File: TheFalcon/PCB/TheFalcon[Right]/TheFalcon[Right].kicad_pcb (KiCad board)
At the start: 4 copper layers, 173.3 x 142.5 mm, 36 parts

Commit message: Save
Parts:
- added C1: 10u, Capacitor_SMD:C_0805_2012Metric, B.Cu at (170.6, 34.7)
- added C10: 22u, Capacitor_SMD:C_1206_3216Metric, B.Cu at (95.3, 32.8)
- added C11: 22u, Capacitor_SMD:C_1206_3216Metric, B.Cu at (95.5, 43.2)
- added C12: 10p, Capacitor_SMD:C_0402_1005Metric, B.Cu at (186.9, 36.5)
- added C13: 100n, Capacitor_SMD:C_0402_1005Metric, B.Cu at (205.1, 39.2)
- added C14: 10p, Capacitor_SMD:C_0402_1005Metric, B.Cu at (186.9, 38.8)
- added C15: 100n, Capacitor_SMD:C_0402_1005Metric, B.Cu at (172.8, 134.6)
- added C16: 100n, Capacitor_SMD:C_0402_1005Metric, B.Cu at (143.5, 134.1)
- added C17: 1u, Capacitor_SMD:C_0603_1608Metric, B.Cu at (141.9, 133.8)
- added C2: 100n, Capacitor_SMD:C_0402_1005Metric, B.Cu at (180.8, 31.8)
- added C3: 100n, Capacitor_SMD:C_0402_1005Metric, B.Cu at (175.4, 43.6)
- added C4: 100n, Capacitor_SMD:C_0402_1005Metric, B.Cu at (184.0, 34.5)
- added C5: 100n, Capacitor_SMD:C_0402_1005Metric, B.Cu at (172.2, 35.2)
- added C6: 10n, Capacitor_SMD:C_0402_1005Metric, B.Cu at (177.4, 46.6)
- added C7: 1u, Capacitor_SMD:C_0603_1608Metric, B.Cu at (177.4, 48.0)
- added C8: 100n, Capacitor_SMD:C_0402_1005Metric, B.Cu at (178.0, 43.8)
- added C9: 1u, Capacitor_SMD:C_0603_1608Metric, B.Cu at (178.4, 45.2)
- added D1: Diode, Diode_SMD:Nexperia_CFP3_SOD-123W, B.Cu at (212.6, 47.0)
- added D10: Diode, Diode_SMD:D_SOD-123, B.Cu at (174.1, 61.2)
- added D11: Diode, Diode_SMD:D_SOD-123, B.Cu at (155.0, 56.3)
- added D12: Diode, Diode_SMD:D_SOD-123, B.Cu at (135.9, 62.3)
- added D13: Diode, Diode_SMD:D_SOD-123, B.Cu at (117.3, 65.4)
- added D14: Diode, Diode_SMD:D_SOD-123, B.Cu at (98.0, 65.3)
- added D15: Diode, Diode_SMD:D_SOD-123, B.Cu at (212.5, 84.9)
- added D16: Diode, Diode_SMD:D_SOD-123, B.Cu at (193.5, 84.9)
- added D17: Diode, Diode_SMD:D_SOD-123, B.Cu at (174.4, 80.2)
- added D18: Diode, Diode_SMD:D_SOD-123, B.Cu at (155.0, 75.3)
- added D19: Diode, Diode_SMD:D_SOD-123, B.Cu at (136.0, 81.3)
- added D2: Diode, Diode_SMD:D_SOD-123, B.Cu at (193.3, 46.9)
- added D20: Diode, Diode_SMD:D_SOD-123, B.Cu at (117.1, 84.3)
- added D21: Diode, Diode_SMD:D_SOD-123, B.Cu at (98.0, 84.2)
- added D22: Diode, Diode_SMD:D_SOD-123, B.Cu at (212.8, 103.8)
- added D23: Diode, Diode_SMD:D_SOD-123, B.Cu at (193.5, 104.0)
- added D24: Diode, Diode_SMD:D_SOD-123, B.Cu at (174.2, 99.0)
- added D25: Diode, Diode_SMD:D_SOD-123, B.Cu at (155.4, 94.4)
- added D26: Diode, Diode_SMD:D_SOD-123, B.Cu at (136.1, 100.4)
- added D27: Diode, Diode_SMD:D_SOD-123, B.Cu at (117.0, 103.5)
- added D28: Diode, Diode_SMD:D_SOD-123, B.Cu at (97.8, 103.6)
- added D29: Diode, Diode_SMD:D_SOD-123, B.Cu at (212.1, 123.0)
- added D3: Diode, Diode_SMD:D_SOD-123, B.Cu at (174.2, 48.8)
- added D30: Diode, Diode_SMD:D_SOD-123, B.Cu at (193.4, 123.1)
- added D31: Diode, Diode_SMD:D_SOD-123, B.Cu at (174.1, 118.2)
- added D32: Diode, Diode_SMD:D_SOD-123, B.Cu at (155.3, 113.6)
- added D33: Diode, Diode_SMD:D_SOD-123, B.Cu at (136.0, 119.4)
- added D34: Diode, Diode_SMD:D_SOD-123, B.Cu at (113.3, 124.4)
- added D35: Diode, Diode_SMD:D_SOD-123, B.Cu at (94.7, 140.6)
- added D36: Diode, Diode_SMD:D_SOD-123, B.Cu at (73.9, 148.9)
- added D39: LED, LED_SMD:LED_0805_2012Metric, B.Cu at (103.6, 42.6)
- added D4: Diode, Diode_SMD:D_SOD-123, B.Cu at (154.7, 40.6)
- added D5: Diode, Diode_SMD:D_SOD-123, B.Cu at (136.1, 43.2)
- added D6: Diode, Diode_SMD:D_SOD-123, B.Cu at (117.0, 49.5)
- added D7: Diode, Diode_SMD:D_SOD-123, B.Cu at (98.2, 49.6)
- added D8: Diode, Diode_SMD:D_SOD-123, B.Cu at (212.6, 65.8)
- added D9: Diode, Diode_SMD:D_SOD-123, B.Cu at (193.3, 65.8)
- added F1: 500mA, Fuse:Fuse_1206_3216Metric, B.Cu at (88.1, 35.0)
- added H1: MountingHole_Pad, MountingHole:MountingHole_2.2mm_M2_Pad, B.Cu at (214.8, 35.3)
- added H2: MountingHole_Pad, MountingHole:MountingHole_2.2mm_M2_Pad, B.Cu at (230.1, 31.2)
- added H3: MountingHole_Pad, MountingHole:MountingHole_2.2mm_M2_Pad, B.Cu at (230.6, 2.30)
- added H4: MountingHole_Pad, MountingHole:MountingHole_2.2mm_M2_Pad, B.Cu at (230.6, 8.25)
- added H5: MountingHole_Pad, MountingHole:MountingHole_2.2mm_M2_Pad, B.Cu at (230.6, 14.2)
- added H6: MountingHole_Pad, MountingHole:MountingHole_2.2mm_M2_Pad, B.Cu at (230.6, 20.1)
- added IC1: IS31FL3729-QFLS4-TR, SamacSys_Parts:QFN40P400X400X80-33N-D, B.Cu at (146.8, 135.7)
- added J1: Conn_01x01, Connector_Wire:SolderWire-0.1sqmm_1x01_D0.4mm_OD1mm, B.Cu at (172.8, 16.9)
- added J2: Conn_01x01, Connector_Wire:SolderWire-0.1sqmm_1x01_D0.4mm_OD1mm, B.Cu at (172.8, 20.5)
- added J3: Conn_01x01, Connector_Wire:SolderWire-0.1sqmm_1x01_D0.4mm_OD1mm, B.Cu at (169.2, 16.9)
- added J4: Conn_01x01, Connector_Wire:SolderWire-0.1sqmm_1x01_D0.4mm_OD1mm, B.Cu at (169.2, 20.5)
- added J5: Conn_01x04_Pin, Connector_Wire:SolderWire-1sqmm_1x04_P5.4mm_D1.4mm_OD2.7mm, B.Cu at (175.3, 6.10)
- added J6: Conn_01x01, Connector_Wire:SolderWire-0.1sqmm_1x01_D0.4mm_OD1mm, B.Cu at (105.6, 32.9)
- added J7: Conn_01x01, Connector_Wire:SolderWire-0.1sqmm_1x01_D0.4mm_OD1mm, B.Cu at (100.9, 32.8)
- added J8: Conn_01x01, Connector_Wire:SolderWirePad_1x01_SMD_1x2mm, B.Cu at (144.0, 128.0)
- added R1: 20, Resistor_SMD:R_0603_1608Metric, B.Cu at (213.1, 55.6)
- added R10: 51, Resistor_SMD:R_0603_1608Metric, B.Cu at (212.6, 59.6)
- added R11: 20, Resistor_SMD:R_0603_1608Metric, B.Cu at (196.4, 78.1)
- added R12: 20, Resistor_SMD:R_0603_1608Metric, B.Cu at (194.1, 78.3)
- added R13: 51, Resistor_SMD:R_0603_1608Metric, B.Cu at (186.7, 82.6)
- added R14: 20, Resistor_SMD:R_0603_1608Metric, B.Cu at (139.0, 93.9)
- added R15: 20, Resistor_SMD:R_0603_1608Metric, B.Cu at (136.8, 95.1)
- added R16: 51, Resistor_SMD:R_0603_1608Metric, B.Cu at (129.1, 98.1)
- added R17: 20, Resistor_SMD:R_0603_1608Metric, B.Cu at (86.8, 124.3)
- added R18: 20, Resistor_SMD:R_0603_1608Metric, B.Cu at (92.6, 124.4)
- added R19: 51, Resistor_SMD:R_0603_1608Metric, B.Cu at (89.9, 124.4)
- added R2: 10k, Resistor_SMD:R_0603_1608Metric, B.Cu at (143.8, 131.4)
- added R20: 20, Resistor_SMD:R_0603_1608Metric, B.Cu at (159.3, 130.6)
- added R21: 20, Resistor_SMD:R_0603_1608Metric, B.Cu at (160.1, 133.2)
- added R22: 51, Resistor_SMD:R_0603_1608Metric, B.Cu at (160.1, 134.8)
- added R23: 0, Resistor_SMD:R_0603_1608Metric_Pad0.98x0.95mm_HandSolder, B.Cu at (143.6, 129.6)
- added R3: 4k7, Resistor_SMD:R_0603_1608Metric, B.Cu at (160.8, 36.8)
- added R4: 4k7, Resistor_SMD:R_0603_1608Metric, B.Cu at (162.4, 38.5)
- added R5: 1k5, Resistor_SMD:R_0603_1608Metric, B.Cu at (108.4, 42.6)
- added R6: 5.1k, Resistor_SMD:R_0603_1608Metric, B.Cu at (210.6, 36.4)
- added R7: 5.1k, Resistor_SMD:R_0603_1608Metric, B.Cu at (211.3, 38.9)
- added R8: 100k, Resistor_SMD:R_0603_1608Metric, B.Cu at (171.3, 134.9)
- added R9: 20, Resistor_SMD:R_0603_1608Metric, B.Cu at (213.2, 57.4)
- added RGB1: T36K3BGR-05D000121U1930, SamacSys_Parts:T36K3BGR05D000121U1930_MODEL_INVERTED, F.Cu at (205.4, 58.3)
- added RGB10: T36K3BGR-05D000121U1930, SamacSys_Parts:T36K3BGR05D000121U1930_MODEL_INVERTED, F.Cu at (167.5, 72.7)
- added RGB11: T36K3BGR-05D000121U1930, SamacSys_Parts:T36K3BGR05D000121U1930_MODEL_INVERTED, F.Cu at (148.4, 67.7)
- added RGB12: T36K3BGR-05D000121U1930, SamacSys_Parts:T36K3BGR05D000121U1930_MODEL_INVERTED, F.Cu at (129.3, 73.7)
- added RGB13: T36K3BGR-05D000121U1930, SamacSys_Parts:T36K3BGR05D000121U1930_MODEL_INVERTED, F.Cu at (110.2, 76.7)
- added RGB14: T36K3BGR-05D000121U1930, SamacSys_Parts:T36K3BGR05D000121U1930_MODEL_INVERTED, F.Cu at (91.1, 76.7)
- added RGB15: T36K3BGR-05D000121U1930, SamacSys_Parts:T36K3BGR05D000121U1930_MODEL_INVERTED, F.Cu at (205.7, 96.4)
- added RGB16: T36K3BGR-05D000121U1930, SamacSys_Parts:T36K3BGR05D000121U1930_MODEL_INVERTED, F.Cu at (186.6, 96.4)
- added RGB17: T36K3BGR-05D000121U1930, SamacSys_Parts:T36K3BGR05D000121U1930_MODEL_INVERTED, F.Cu at (167.5, 91.7)
- added RGB18: T36K3BGR-05D000121U1930, SamacSys_Parts:T36K3BGR05D000121U1930_MODEL_INVERTED, F.Cu at (148.4, 86.9)
- added RGB19: T36K3BGR-05D000121U1930, SamacSys_Parts:T36K3BGR05D000121U1930_MODEL_INVERTED, F.Cu at (129.3, 92.9)
- added RGB2: T36K3BGR-05D000121U1930, SamacSys_Parts:T36K3BGR05D000121U1930_MODEL_INVERTED, F.Cu at (186.3, 58.2)
- added RGB20: T36K3BGR-05D000121U1930, SamacSys_Parts:T36K3BGR05D000121U1930_MODEL_INVERTED, F.Cu at (110.2, 95.9)
- added RGB21: T36K3BGR-05D000121U1930, SamacSys_Parts:T36K3BGR05D000121U1930_MODEL_INVERTED, F.Cu at (91.3, 95.9)
- added RGB22: T36K3BGR-05D000121U1930, SamacSys_Parts:T36K3BGR05D000121U1930_MODEL_INVERTED, F.Cu at (205.7, 115.2)
- added RGB23: T36K3BGR-05D000121U1930, SamacSys_Parts:T36K3BGR05D000121U1930_MODEL_INVERTED, F.Cu at (186.3, 115.4)
- added RGB24: T36K3BGR-05D000121U1930, SamacSys_Parts:T36K3BGR05D000121U1930_MODEL_INVERTED, F.Cu at (167.5, 110.7)
- added RGB25: T36K3BGR-05D000121U1930, SamacSys_Parts:T36K3BGR05D000121U1930_MODEL_INVERTED, F.Cu at (148.1, 105.9)
- added RGB26: T36K3BGR-05D000121U1930, SamacSys_Parts:T36K3BGR05D000121U1930_MODEL_INVERTED, F.Cu at (129.3, 111.9)
- added RGB27: T36K3BGR-05D000121U1930, SamacSys_Parts:T36K3BGR05D000121U1930_MODEL_INVERTED, F.Cu at (110.2, 114.9)
- added RGB28: T36K3BGR-05D000121U1930, SamacSys_Parts:T36K3BGR05D000121U1930_MODEL_INVERTED, F.Cu at (91.1, 114.9)
- added RGB29: T36K3BGR-05D000121U1930, SamacSys_Parts:T36K3BGR05D000121U1930_MODEL_INVERTED, F.Cu at (205.4, 134.4)
- added RGB3: T36K3BGR-05D000121U1930, SamacSys_Parts:T36K3BGR05D000121U1930_MODEL_INVERTED, F.Cu at (167.5, 53.7)
- added RGB30: T36K3BGR-05D000121U1930, SamacSys_Parts:T36K3BGR05D000121U1930_MODEL_INVERTED, F.Cu at (186.3, 134.4)
- added RGB31: T36K3BGR-05D000121U1930, SamacSys_Parts:T36K3BGR05D000121U1930_MODEL_INVERTED, F.Cu at (167.2, 129.7)
- added RGB32: T36K3BGR-05D000121U1930, SamacSys_Parts:T36K3BGR05D000121U1930_MODEL_INVERTED, F.Cu at (148.4, 124.9)
- added RGB33: T36K3BGR-05D000121U1930, SamacSys_Parts:T36K3BGR05D000121U1930_MODEL_INVERTED, F.Cu at (129.3, 130.9)
- added RGB34: T36K3BGR-05D000121U1930, SamacSys_Parts:T36K3BGR05D000121U1930_MODEL_INVERTED, F.Cu at (106.6, 136.9)
- added RGB35: T36K3BGR-05D000121U1930, SamacSys_Parts:T36K3BGR05D000121U1930_MODEL_INVERTED, F.Cu at (80.8, 142.7)
- added RGB36: T36K3BGR-05D000121U1930, SamacSys_Parts:T36K3BGR05D000121U1930_MODEL_INVERTED, F.Cu at (60.4, 154.2)
- added RGB4: T36K3BGR-05D000121U1930, SamacSys_Parts:T36K3BGR05D000121U1930_MODEL_INVERTED, F.Cu at (148.4, 48.7)
- added RGB5: T36K3BGR-05D000121U1930, SamacSys_Parts:T36K3BGR05D000121U1930_MODEL_INVERTED, F.Cu at (129.3, 54.7)
- added RGB6: T36K3BGR-05D000121U1930, SamacSys_Parts:T36K3BGR05D000121U1930_MODEL_INVERTED, F.Cu at (110.4, 57.7)
- added RGB7: T36K3BGR-05D000121U1930, SamacSys_Parts:T36K3BGR05D000121U1930_MODEL_INVERTED, F.Cu at (91.3, 57.9)
- added RGB8: T36K3BGR-05D000121U1930, SamacSys_Parts:T36K3BGR05D000121U1930_MODEL_INVERTED, F.Cu at (205.5, 77.4)
- added RGB9: T36K3BGR-05D000121U1930, SamacSys_Parts:T36K3BGR05D000121U1930_MODEL_INVERTED, F.Cu at (186.6, 77.4)
- added SW1: SW_Push, Button_Switch_SMD:SW_SPST_B3U-1000P, B.Cu at (207.8, 37.2)
- added SW2: SW_Push, Button_Switch_SMD:SW_SPST_B3U-1000P, B.Cu at (202.5, 37.0)
- added U1: STM32G431CBTx, Package_QFP:LQFP-48_7x7mm_P0.5mm, B.Cu at (178.2, 37.8)
- added U3: USBLC6-2P6, Package_TO_SOT_SMD:SOT-666, B.Cu at (88.9, 37.8)
- added U4: AMS1117-3.3, Package_TO_SOT_SMD:SOT-223-3_TabPin2, B.Cu at (97.0, 38.1)
- added USB2: USB_C_Receptacle_USB2.0_16P, Connector_USB:USB_C_Receptacle_G-Switch_GT-USB-7010ASV, B.Cu at (79.6, 37.7)
- added Y1: X322516MOB4SI, SamacSys_Parts:X322516MOB4SI, B.Cu at (190.4, 37.0)
- moved S9 211.5 mm to (185.7, 72.1)
- moved S1 211.5 mm to (204.7, 53.1)
- moved S10 211.5 mm to (166.6, 67.3)
- moved S11 211.5 mm to (147.6, 62.6)
- moved S12 211.5 mm to (128.5, 68.6)
- moved S13 211.5 mm to (109.5, 71.6)
- moved S14 211.5 mm to (90.4, 71.6)
- moved S15 211.5 mm to (204.7, 91.2)
- moved S17 211.5 mm to (166.6, 86.4)
- moved S22 211.5 mm to (204.7, 110.2)
- moved S25 211.5 mm to (147.6, 100.7)
- moved S26 211.5 mm to (128.5, 106.7)
- moved S27 211.5 mm to (109.5, 109.7)
- moved S28 211.5 mm to (90.4, 109.7)
- moved S3 211.5 mm to (166.6, 48.3)
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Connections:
- S1 pad 1: Col0 -> Col6
- S10 pad 1: Col2 -> Col4
- S12 pad 1: Col4 -> Col2
- S13 pad 1: Col5 -> Col1
- S14 pad 1: Col6 -> Col0
- S15 pad 1: Col0 -> Col6
- S16 pad 1: Col1 -> Col5
- S17 pad 1: Col2 -> Col4
- S19 pad 1: Col4 -> Col2
- S2 pad 1: Col1 -> Col5
- S20 pad 1: Col5 -> Col1
- S21 pad 1: Col6 -> Col0
- S22 pad 1: Col0 -> Col6
- S23 pad 1: Col1 -> Col5
- S24 pad 1: Col2 -> Col4
- S26 pad 1: Col4 -> Col2
- S27 pad 1: Col5 -> Col1
- S28 pad 1: Col6 -> Col0
- S29 pad 1: Col0 -> Col6
- S3 pad 1: Col2 -> Col4
- S30 pad 1: Col1 -> Col5
- S31 pad 1: Col2 -> Col4
- S33 pad 1: Col4 -> Col2
- S34 pad 1: Col4 -> Col2
- S35 pad 1: Col5 -> Col1
- S36 pad 1: Col6 -> Col0
- S5 pad 1: Col4 -> Col2
- S6 pad 1: Col5 -> Col1
- S7 pad 1: Col6 -> Col0
- S8 pad 1: Col0 -> Col6
- S9 pad 1: Col1 -> Col5
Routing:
- net Row3: track 0.00 -> 235.3 mm, vias 0 -> 8
- net ThumbRow: track 0.00 -> 224.0 mm, vias 0 -> 2
- net Row4: track 0.00 -> 217.0 mm, vias 0 -> 6
- net Row2: track 0.00 -> 209.6 mm, vias 0 -> 8
- net /RGB Array/G_RGB_ROW_4: track 0.00 -> 208.7 mm, vias 0 -> 8
- net /RGB Array/R_RGB_ROW_4: track 0.00 -> 206.3 mm, vias 0 -> 9
- net Col0: track 0.00 -> 205.7 mm, vias 0 -> 2
- net /RGB Array/B_RGB_ROW_4: track 0.00 -> 202.9 mm, vias 0 -> 9
- net +3.3V: track 0.00 -> 181.4 mm, vias 0 -> 4
- net Col1: track 0.00 -> 180.9 mm, vias 0 -> 2
- net Row0: track 0.00 -> 173.7 mm, vias 0 -> 7
- net Row1: track 0.00 -> 171.4 mm, vias 0 -> 7
- net /RGB Array/G_RGB_ROW_3: track 0.00 -> 167.2 mm, vias 0 -> 7
- net +5V: track 0.00 -> 166.6 mm, vias 0 -> 5
- net /RGB Array/G_RGB_ROW_1: track 0.00 -> 157.2 mm, vias 0 -> 7
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- added copper zone on B.Cu, net +3.3V
- added copper zone on B.Cu, net +5V
- added copper zone on F.Cu, net +5V
- added copper zone on B.Cu, net GND
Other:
- board text added: "PA15"
- board text added: "X"

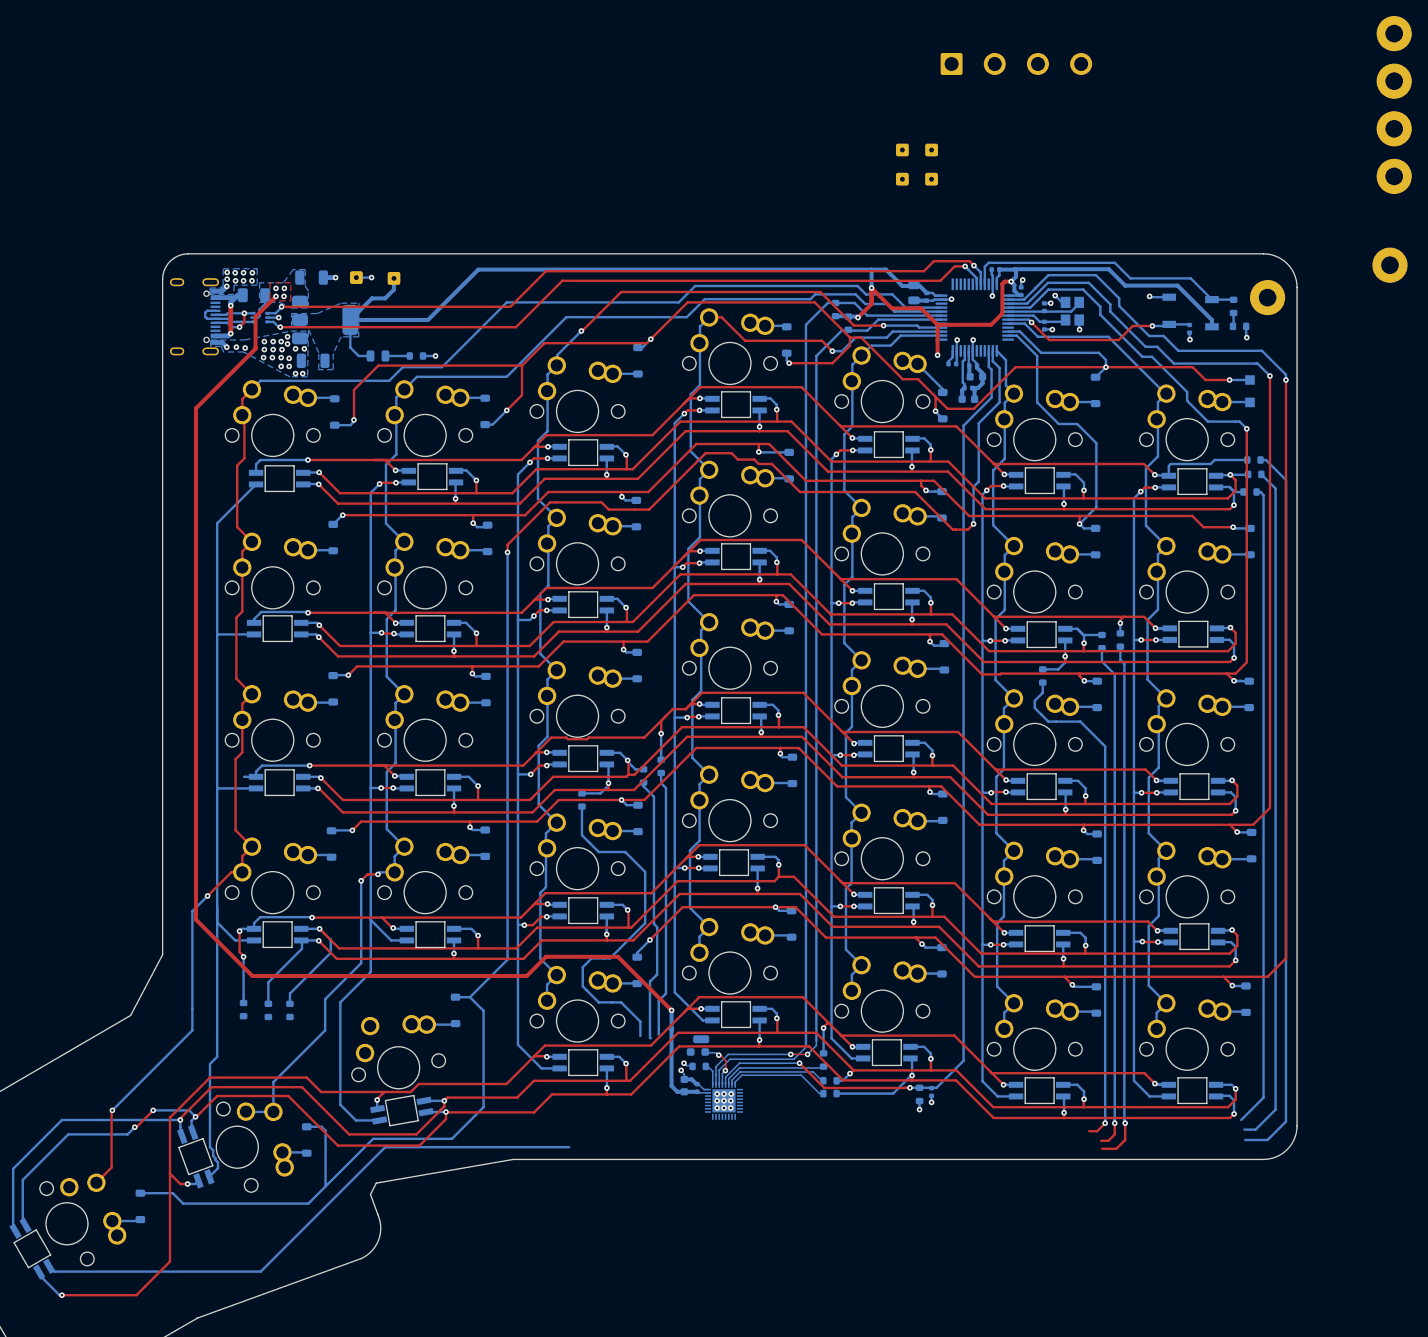
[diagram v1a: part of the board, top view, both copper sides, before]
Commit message: Right Side Done
Need to check but right side looks good
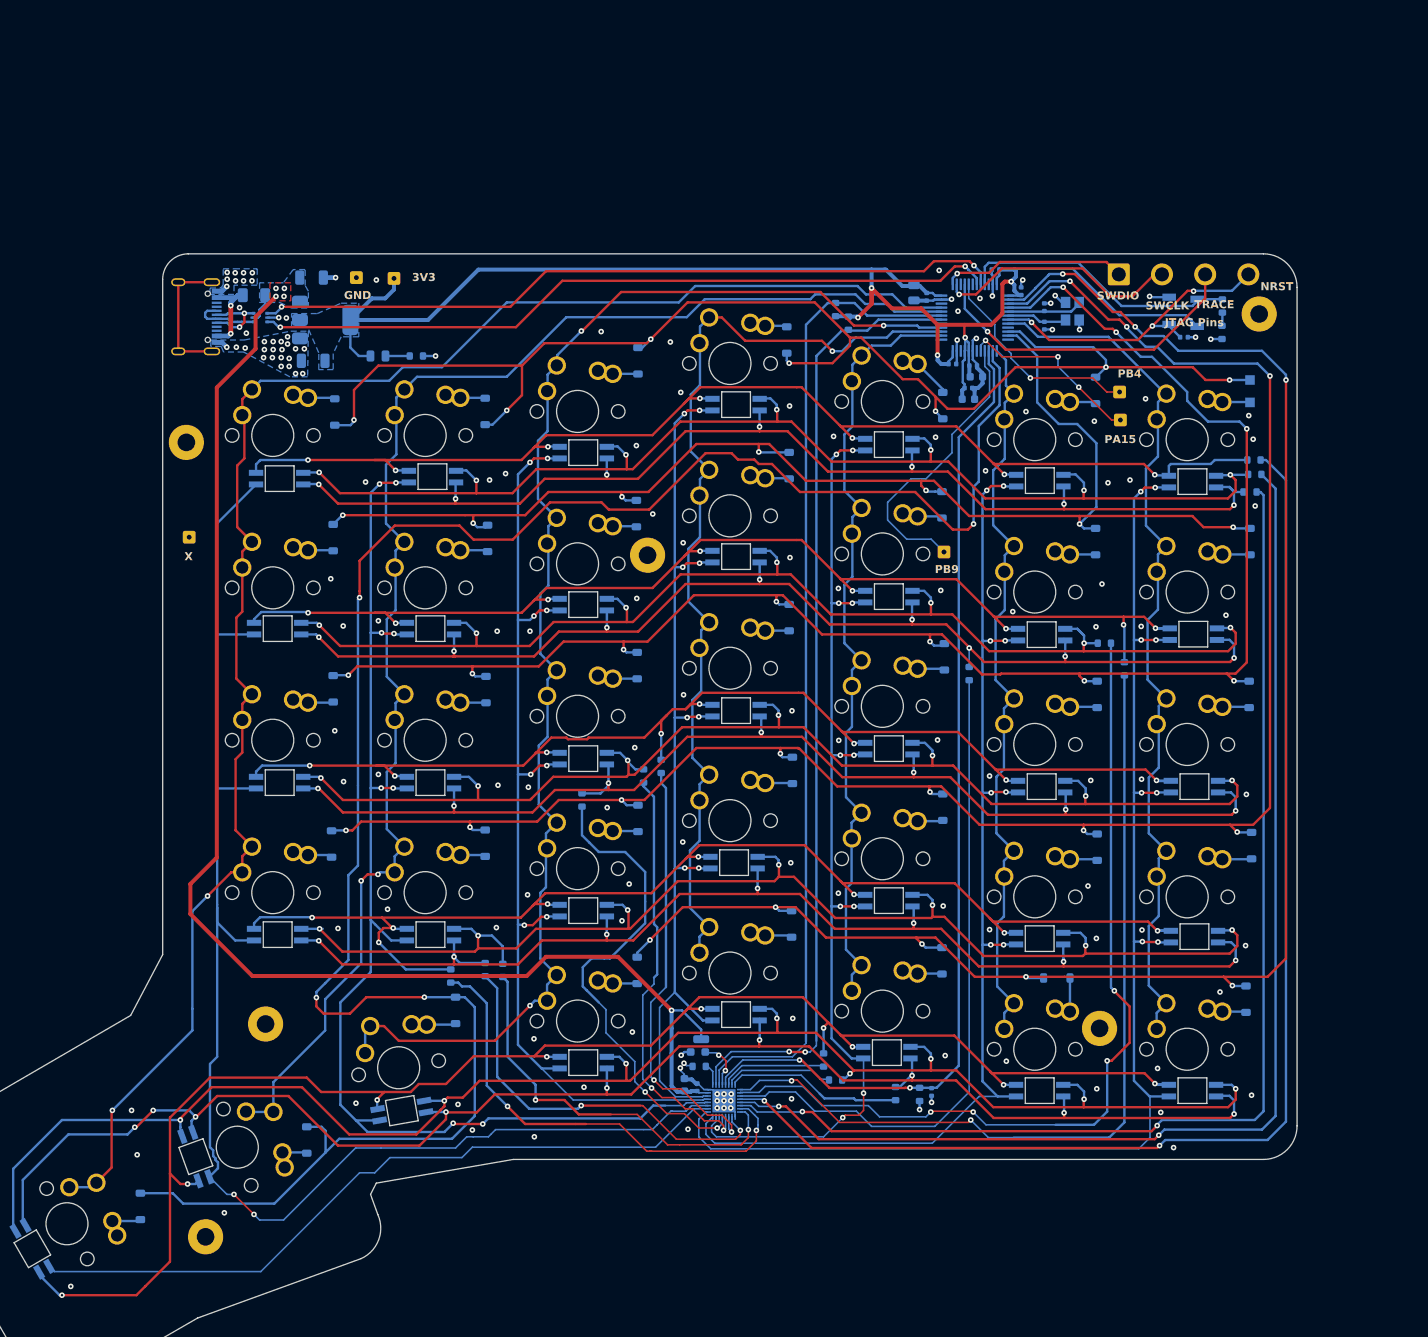
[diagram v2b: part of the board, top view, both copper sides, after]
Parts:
- moved H2 191.5 mm to (82.0, 152.7)
- moved H6 176.4 mm to (89.5, 126.1)
- moved H4 157.6 mm to (79.7, 53.4)
- moved H5 118.3 mm to (193.8, 126.7)
- moved H3 113.8 mm to (137.3, 67.5)
- moved J3 101.4 mm to (80.0, 65.2)
- moved J4 46.9 mm to (174.3, 67.1)
- moved J1 41.2 mm to (196.4, 50.6)
- moved J2 35.5 mm to (196.3, 47.1)
- moved J5 33.6 mm to (196.2, 32.4)
- moved R19 27.6 mm to (117.0, 119.3)
- moved R18 27.1 mm to (119.2, 119.4)
- moved R17 26.2 mm to (112.7, 120.1)
- moved R13 9.20 mm to (177.5, 82.3)
- moved R22 8.20 mm to (168.3, 134.8), turned to -90 degrees
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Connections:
- RGB1 pad 2: /RGB Array/SW8 -> /RGB Array/SW6
- RGB10 pad 2: /RGB Array/SW6 -> /RGB Array/SW8
- RGB11 pad 2: /RGB Array/SW5 -> /RGB Array/SW1
- RGB12 pad 2: /RGB Array/SW4 -> /RGB Array/SW2
- RGB14 pad 2: /RGB Array/SW2 -> /RGB Array/SW4
- RGB15 pad 2: /RGB Array/SW8 -> /RGB Array/SW6
- RGB17 pad 2: /RGB Array/SW6 -> /RGB Array/SW8
- RGB18 pad 2: /RGB Array/SW5 -> /RGB Array/SW1
- RGB19 pad 2: /RGB Array/SW4 -> /RGB Array/SW2
- RGB21 pad 2: /RGB Array/SW2 -> /RGB Array/SW4
- RGB22 pad 2: /RGB Array/SW8 -> /RGB Array/SW6
- RGB24 pad 2: /RGB Array/SW6 -> /RGB Array/SW8
- RGB25 pad 2: /RGB Array/SW5 -> /RGB Array/SW1
- RGB26 pad 2: /RGB Array/SW4 -> /RGB Array/SW2
- RGB28 pad 2: /RGB Array/SW2 -> /RGB Array/SW4
- RGB29 pad 2: /RGB Array/SW8 -> /RGB Array/SW6
- RGB3 pad 2: /RGB Array/SW6 -> /RGB Array/SW8
- RGB31 pad 2: /RGB Array/SW6 -> /RGB Array/SW8
- RGB32 pad 2: /RGB Array/SW5 -> /RGB Array/SW1
- RGB33 pad 2: /RGB Array/SW4 -> /RGB Array/SW2
- RGB35 pad 2: /RGB Array/SW2 -> /RGB Array/SW4
- RGB36 pad 2: /RGB Array/SW1 -> /RGB Array/SW5
- RGB4 pad 2: /RGB Array/SW5 -> /RGB Array/SW1
- RGB5 pad 2: /RGB Array/SW4 -> /RGB Array/SW2
- RGB7 pad 2: /RGB Array/SW2 -> /RGB Array/SW4
- RGB8 pad 2: /RGB Array/SW8 -> /RGB Array/SW6
- U1 pad 17: unconnected-(U1-PB1-Pad17) -> PA15
- U1 pad 39: PA15 -> unconnected-(U1-PA15-Pad39)
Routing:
- net /RGB Array/SW4: track 100.9 -> 177.2 mm, vias 8 -> 2
- net /RGB Array/SW6: track 94.8 -> 163.1 mm
- net /RGB Array/CS7: track 90.5 -> 156.6 mm, vias 0 -> 2
- net /RGB Array/CS8: track 85.1 -> 151.0 mm, vias 0 -> 2
- net /RGB Array/CS9: track 79.9 -> 145.6 mm, vias 0 -> 2
- net /RGB Array/CS10: track 0.00 -> 59.5 mm, vias 0 -> 2
- net /RGB Array/CS11: track 0.00 -> 50.4 mm, vias 0 -> 2
- net /RGB Array/CS12: track 0.00 -> 50.0 mm, vias 0 -> 2
- net /RGB Array/CS5: track 63.7 -> 110.5 mm, vias 1 -> 4
- net /RGB Array/SW3: track 103.8 -> 150.0 mm, vias 6 -> 8
- net /RGB Array/SW1: track 71.7 -> 115.7 mm, vias 0 -> 8
- net /RGB Array/CS4: track 65.6 -> 108.5 mm, vias 1 -> 2
- net /RGB Array/SW7: track 96.2 -> 138.1 mm
- net SYS_JTAG_TRACE: track 0.00 -> 40.9 mm, vias 0 -> 1
- net PB9: track 0.00 -> 36.5 mm
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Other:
- board text added: "3V3"
- board text added: "5V"
- board text added: "GND"
- board text added: "JTAG Pins"
- board text added: "NRST"
- board text added: "PB4"
- board text added: "PB9"
- board text added: "PWR"
- board text added: "SWCLK"
- board text added: "SWDIO"
- board text added: "TRACE"
- board text added: "USB Serial Connection"

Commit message: Save
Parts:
- removed H1, H2, H3, H4, H5, H6: MountingHole_Pad, MountingHole:MountingHole_2.2mm_M2_Pad
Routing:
- net unconnected-(USB2-SHIELD-PadS1): track 17.0 -> 0.00 mm
- net GND: track 55.7 -> 53.8 mm, vias 154 -> 153
- net /RGB Array/SW6: track 163.1 -> 164.4 mm
- net /RGB Array/SW2: track 123.4 -> 124.4 mm
- net /RGB Array/CS5: track 110.5 -> 111.3 mm
- net /RGB Array/CS4: track 108.5 -> 109.2 mm
- net (no net): vias 0 -> 1
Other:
- outline, holes or cut-outs redrawn
- board text added: "SPACER"
